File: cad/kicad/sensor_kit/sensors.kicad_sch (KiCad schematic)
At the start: 6 parts, among them J11 DS18B20, J5 QWIIC_I2C_3, J6 QWIIC_I2C_2, J7 QWIIC_I2C_1, J8 SPI_BREAKOUT

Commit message: adds further sensors to board layout
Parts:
- added D2: 1N4149, Diode_THT:D_DO-35_SOD27_P7.62mm_Horizontal, symbol Diode:1N4149
- added J7: PT1000_RTD, cryoskills_sensor_kit:TerminalBlock_Multicomp_5.08_2way_MP012059, symbol Connector:Screw_Terminal_01x02
- added R21: 3k, Resistor_THT:R_Axial_DIN0204_L3.6mm_D1.6mm_P5.08mm_Horizontal, symbol Device:R
- added R22: 330R, Resistor_THT:R_Axial_DIN0204_L3.6mm_D1.6mm_P5.08mm_Horizontal, symbol Device:R
- added R23: 2.4k, Resistor_THT:R_Axial_DIN0204_L3.6mm_D1.6mm_P5.08mm_Horizontal, symbol Device:R
- added U4: LM334Z, Package_TO_SOT_THT:TO-92_Inline, symbol Reference_Current:LM334Z
- J?: renamed from J11; footprint (none) -> cryoskills_sensor_kit:TerminalBlock_Multicomp_5.08_3way_MP012060; Manufacturer (none) -> Multicomp PRO; MftrPartNo (none) -> MP12060; Supplier (none) -> Farnell; SupplierPartNo (none) -> 4179098
- R?: renamed from R21; footprint (none) -> Resistor_THT:R_Axial_DIN0204_L3.6mm_D1.6mm_P5.08mm_Horizontal
- renumbered J6 to J?, J7 to J?, J8 to J?, J5 to J?
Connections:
- net GND: now also R21.2
- net VCC: now also U4.1
- new net: R22.1, R23.1, U4.2
- new net: D2.2 (A), R22.2, U4.3
- new net ADC_REF+: J7.2 (Pin_2), R21.1
- new net ADC_RTD+: D2.1 (K), J7.1 (Pin_1), R23.2
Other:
- note added: "Alternative is 2.2k if using 1x ADC gain"
- note added: "Decoupling capacitors?"

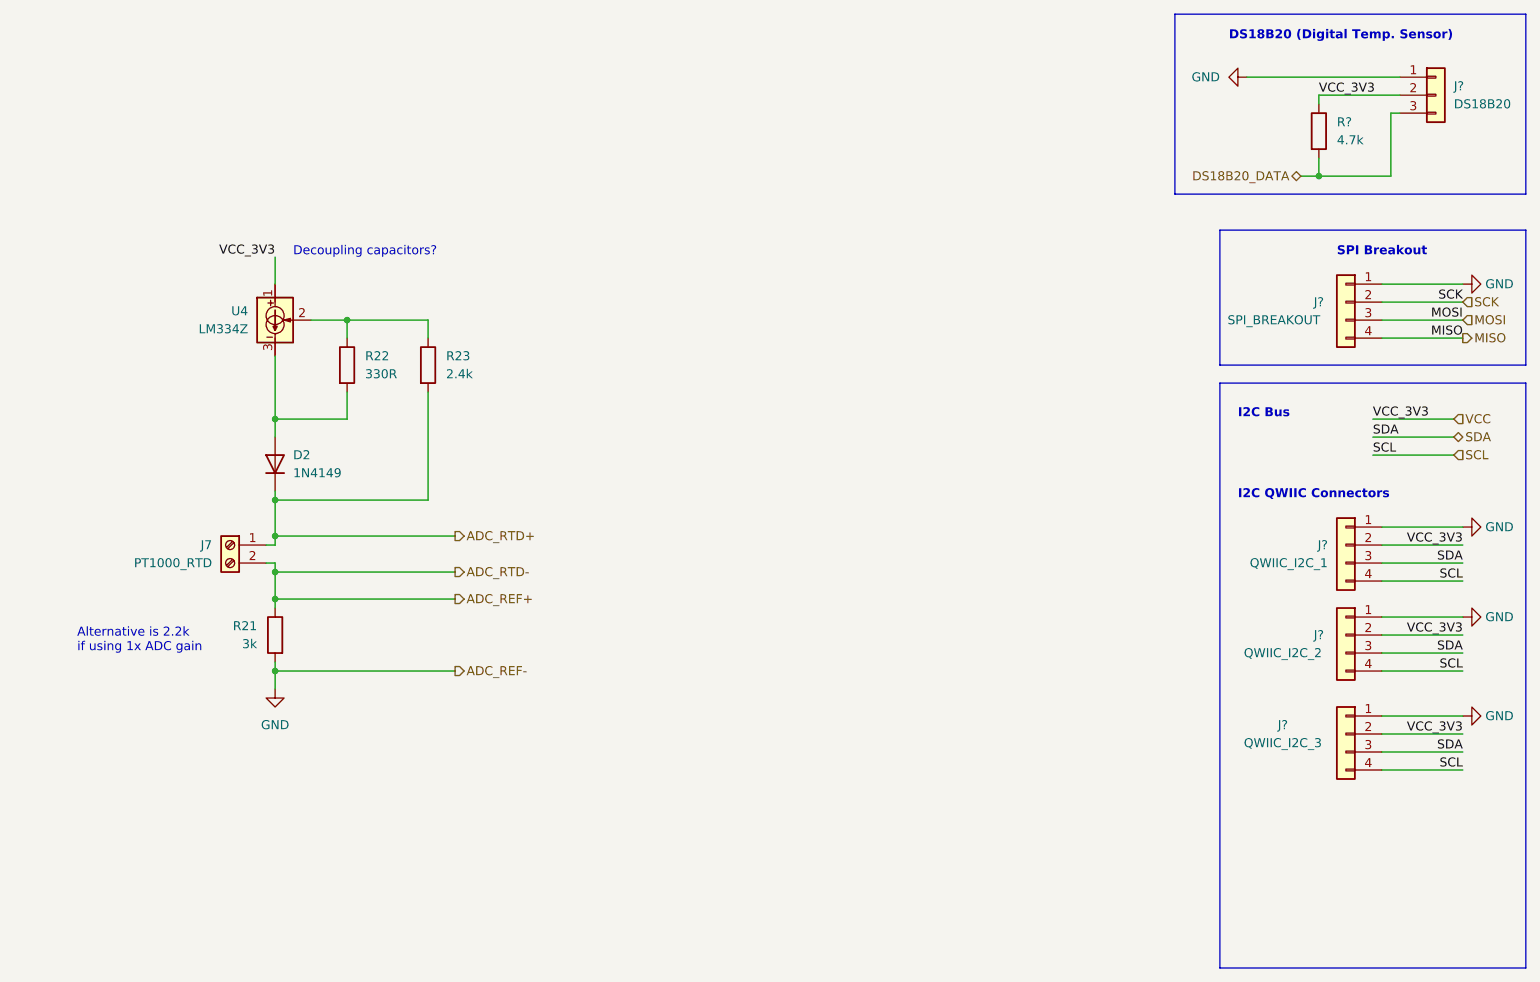
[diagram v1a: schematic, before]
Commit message: updates sensorkit PCB with revised pinout and wheatstone bridge circuit
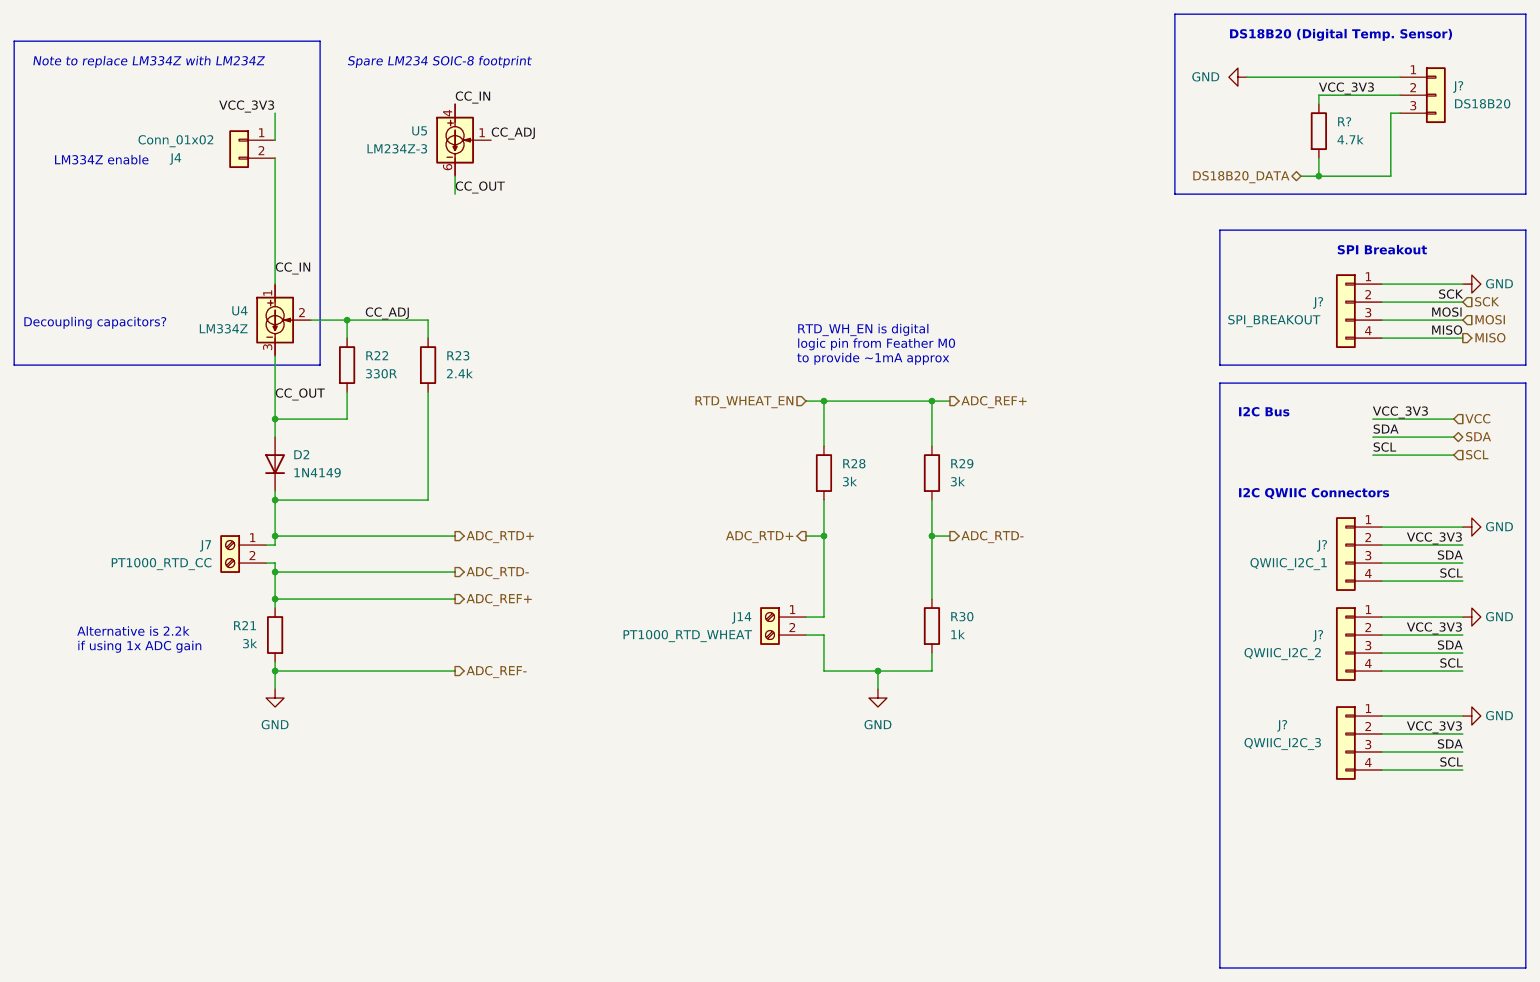
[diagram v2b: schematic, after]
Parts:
- added J14: PT1000_RTD_WHEAT, cryoskills_sensor_kit:TerminalBlock_Multicomp_5.08_2way_MP012059, symbol Connector:Screw_Terminal_01x02
- added J4: Conn_01x02, Connector_PinHeader_2.54mm:PinHeader_1x02_P2.54mm_Vertical, symbol Connector_Generic:Conn_01x02
- added R28, R29: 3k, Resistor_THT:R_Axial_DIN0204_L3.6mm_D1.6mm_P5.08mm_Horizontal, symbol Device:R
- added R30: 1k, Resistor_THT:R_Axial_DIN0204_L3.6mm_D1.6mm_P5.08mm_Horizontal, symbol Device:R
- added U5: LM234Z-3, Package_SO:SOIC-8_3.9x4.9mm_P1.27mm, symbol cryoskills_sensor_kit:LM234Z-3
- J7: value PT1000_RTD -> PT1000_RTD_CC
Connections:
- net ADC_REF+: now also R28.1, R29.1, R29.2, R30.1
- net ADC_RTD+: now also J14.1 (Pin_1), R28.2
- net GND: now also J14.2 (Pin_2), R30.2
- net VCC: now also J4.1 (Pin_1); no longer U4.1
- net CC_ADJ: now reaches R22.1, R23.1, U4.2
- net CC_ADJ: now also U5.1
- net CC_OUT: now reaches D2.2 (A), R22.2, U4.3
- net CC_OUT: now also U5.6
- new net CC_IN: J4.2 (Pin_2), U4.1, U5.4
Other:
- note added: "LM334Z enable"
- note added: "Note to replace LM334Z with LM234Z"
- note added: "RTD_WH_EN is digital logic pin from Feather M0 to provide ~1mA approx"
- note added: "Spare LM234 SOIC-8 footprint"

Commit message: revises sensor board to remove current source and reduce footprint
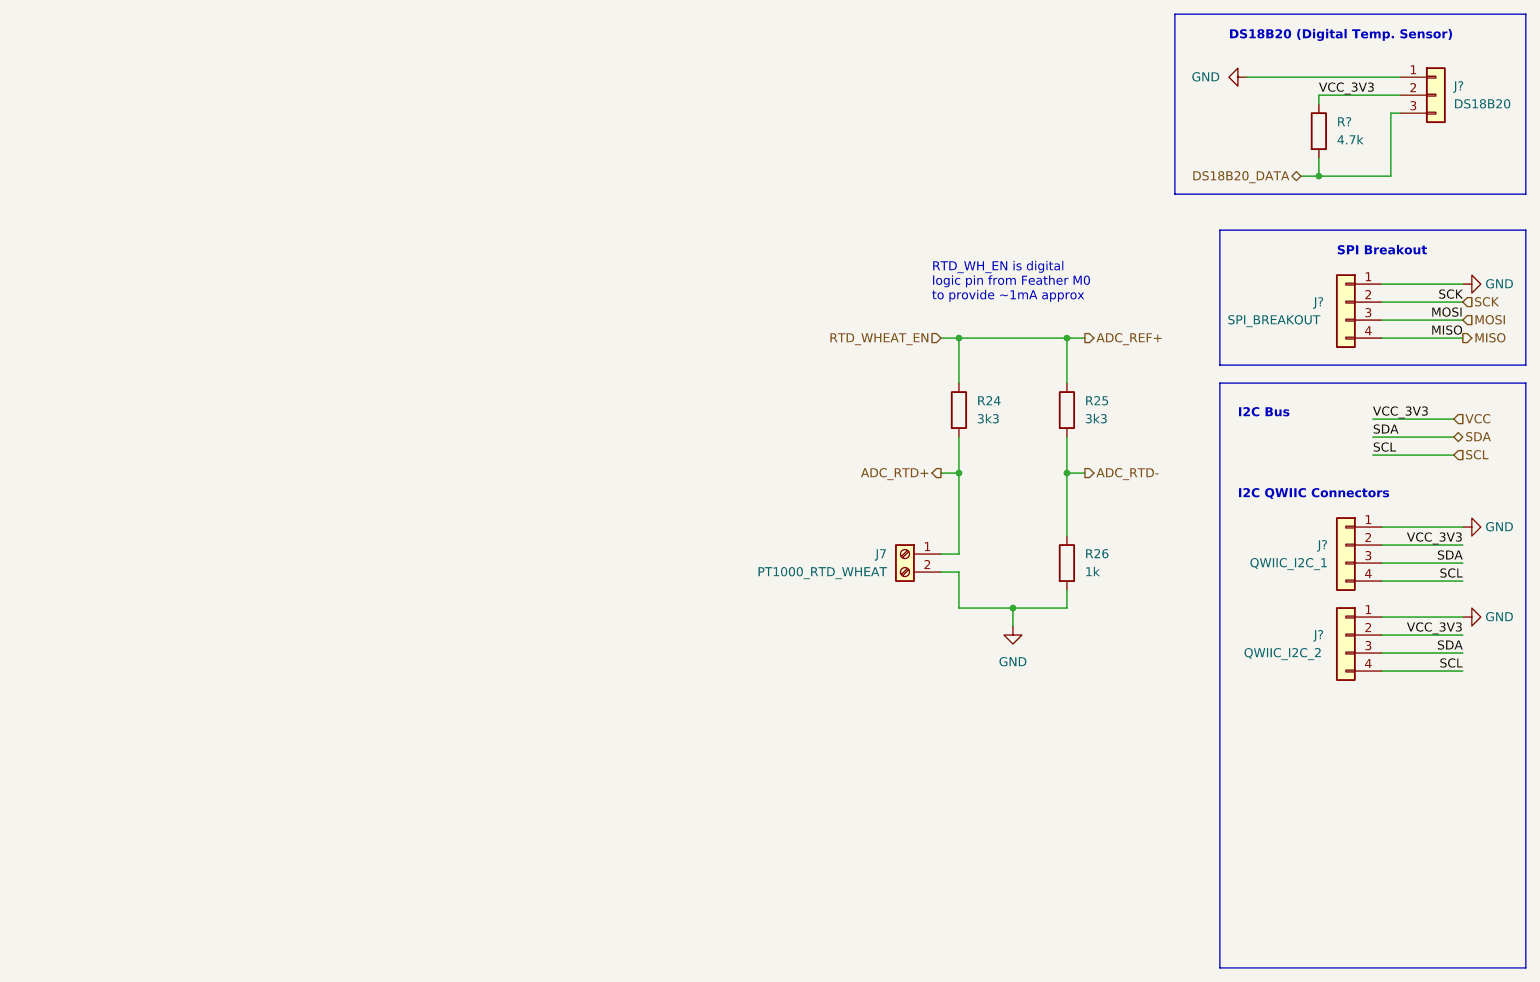
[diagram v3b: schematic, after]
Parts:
- removed D2: 1N4149, Diode_THT:D_DO-35_SOD27_P7.62mm_Horizontal, symbol Diode:1N4149
- removed J4: Conn_01x02, Connector_PinHeader_2.54mm:PinHeader_1x02_P2.54mm_Vertical, symbol Connector_Generic:Conn_01x02
- removed J7: PT1000_RTD_CC, cryoskills_sensor_kit:TerminalBlock_Multicomp_5.08_2way_MP012059, symbol Connector:Screw_Terminal_01x02
- removed J?: QWIIC_I2C_3, Connector_JST:JST_SH_SM04B-SRSS-TB_1x04-1MP_P1.00mm_Horizontal, symbol Connector_Generic:Conn_01x04
- removed R21: 3k, Resistor_THT:R_Axial_DIN0204_L3.6mm_D1.6mm_P5.08mm_Horizontal, symbol Device:R
- removed R22: 330R, Resistor_THT:R_Axial_DIN0204_L3.6mm_D1.6mm_P5.08mm_Horizontal, symbol Device:R
- removed R23: 2.4k, Resistor_THT:R_Axial_DIN0204_L3.6mm_D1.6mm_P5.08mm_Horizontal, symbol Device:R
- removed U4: LM334Z, Package_TO_SOT_THT:TO-92_Inline, symbol Reference_Current:LM334Z
- removed U5: LM234Z-3, Package_SO:SOIC-8_3.9x4.9mm_P1.27mm, symbol cryoskills_sensor_kit:LM234Z-3
- R24: renamed from R28; value 3k -> 3k3
- R25: renamed from R29; value 3k -> 3k3
- renumbered J14 to J7, R30 to R26
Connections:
- net ADC_REF+: no longer R25.2, R26.1
- new net ADC_RTD-: R25.2, R26.1
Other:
- note removed: "Alternative is 2.2k if using 1x ADC gain"
- note removed: "Decoupling capacitors?"
- note removed: "LM334Z enable"
- note removed: "Note to replace LM334Z with LM234Z"
- note removed: "Spare LM234 SOIC-8 footprint"
- moved on the sheet: J7, R24, R25, R26
